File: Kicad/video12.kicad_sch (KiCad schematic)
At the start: 18 parts, among them J1201 DE15HD, U1201 THS7316, U1202 TPD7S019

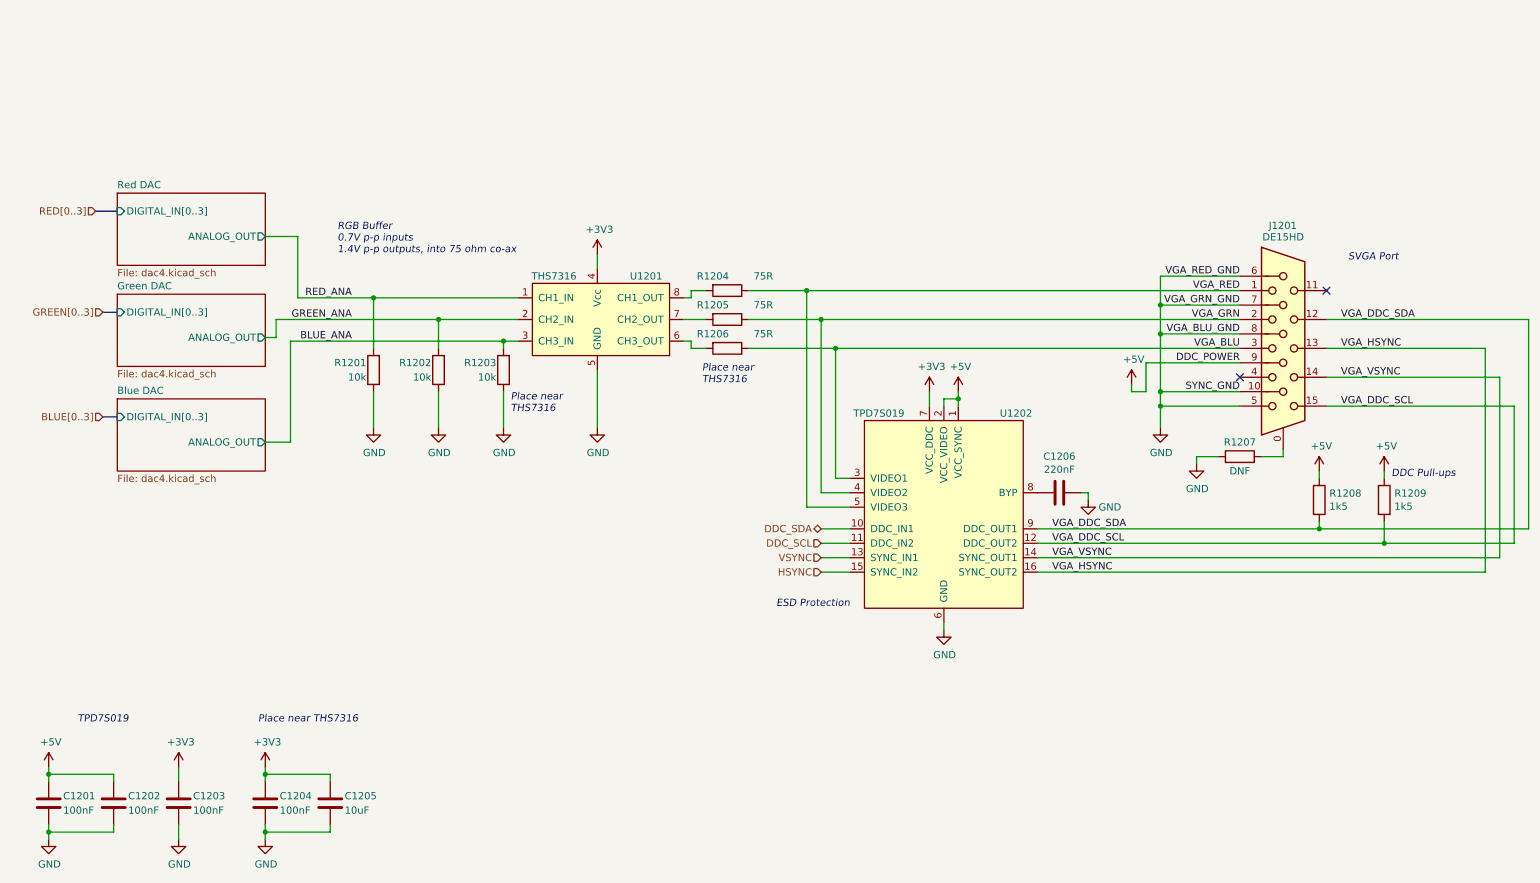
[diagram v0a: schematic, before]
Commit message: Update schematic files to Kicad 6.
Had to fix some symbols which didn't have perfect matches in K6.
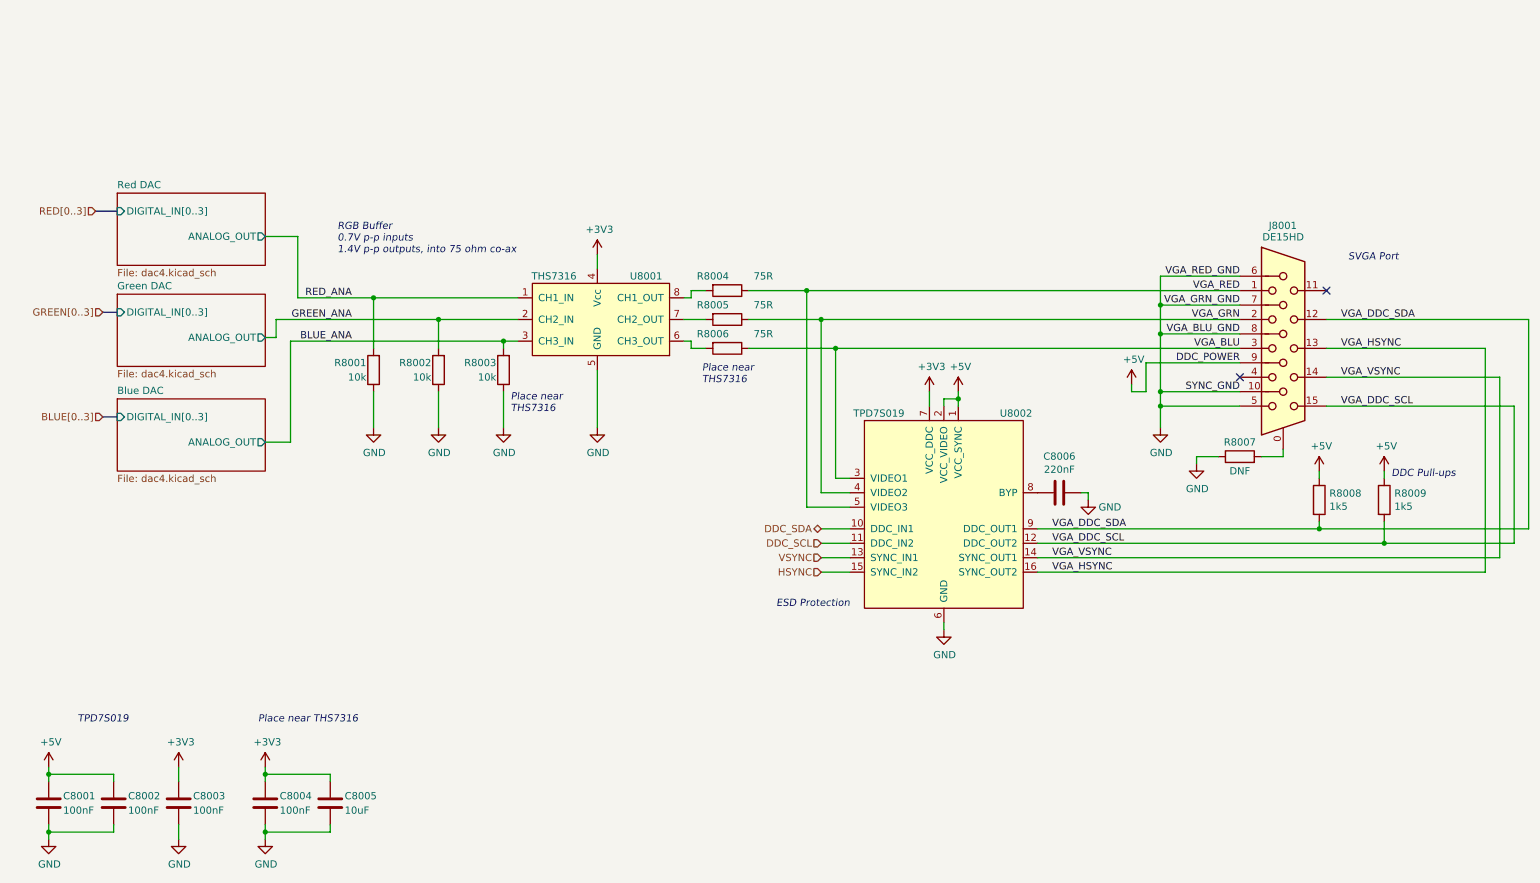
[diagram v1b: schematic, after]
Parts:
- renumbered C1201 to C8001, C1202 to C8002, C1203 to C8003, C1204 to C8004, C1205 to C8005, C1206 to C8006, J1201 to J8001, R1201 to R8001, R1202 to R8002, R1203 to R8003, R1204 to R8004, R1205 to R8005, R1206 to R8006, R1207 to R8007, R1208 to R8008, R1209 to R8009, U1201 to U8001, U1202 to U8002

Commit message: Imported sheets from Neotron Pico.
Standardised on +3V3 not +3.3V
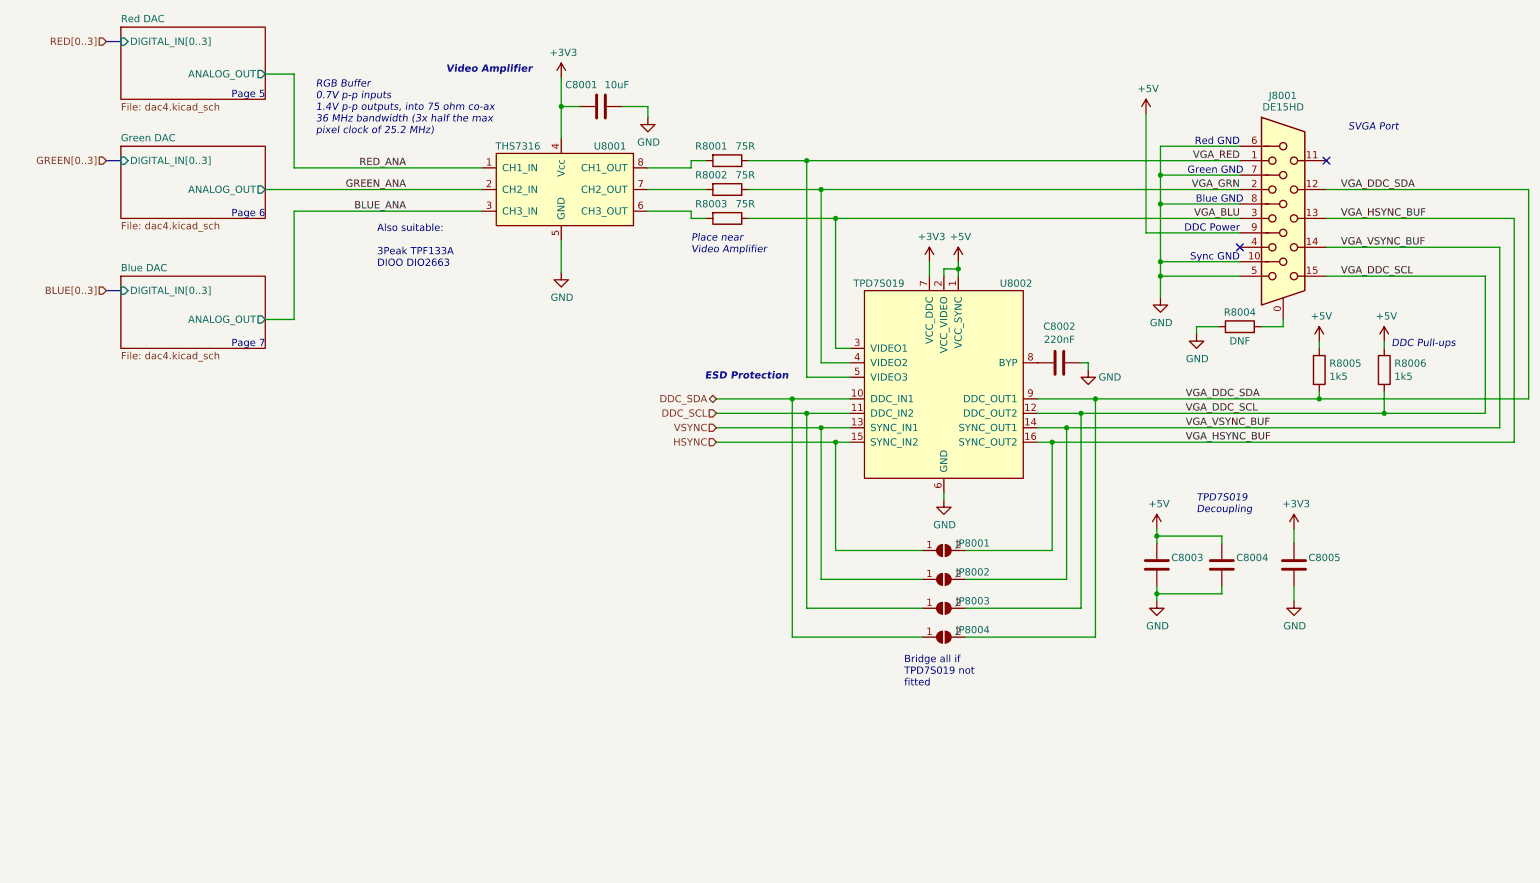
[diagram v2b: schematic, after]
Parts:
- removed C8001, C8002: 100nF, Capacitor_SMD:C_0805_2012Metric_Pad1.18x1.45mm_HandSolder, symbol Device:C
- removed R8001, R8002, R8003: 10k, Resistor_SMD:R_0805_2012Metric_Pad1.20x1.40mm_HandSolder, symbol Device:R
- added C8005: (no value), symbol Device:C
- added JP8001, JP8002, JP8003, JP8004: (no value), symbol Jumper:SolderJumper_2_Open
- C8001: renamed from C8005; JLCPCB Collection (none) -> Basic; MPN CPL-CAP-X5R-0805-10UF-16V -> CL21A106KAYNNNE; Manufacturer CPL -> Samsung; Voltage 10V -> 25V
- C8002: renamed from C8006; Digikey 1276-1093-1-ND -> (none); JLCPCB Collection (none) -> Basic; Tolerance X5R -> X7R
- C8003, C8004: value 100nF -> (none); footprint Capacitor_SMD:C_0805_2012Metric_Pad1.18x1.45mm_HandSolder -> (none); JLCPCB Collection (none) -> Basic; LCSC Part# C49678 -> C15850; MPN CPL-CAP-X7R-0805-100NF-50V -> CL21A106KAYNNNE; Manufacturer CPL -> Samsung; Voltage 10V -> 25V
- R8001: renamed from R8004; Digikey RMCF0805FT75R0-ND -> (none); JLCPCB Collection (none) -> Basic; MPN RMCF0805FT75R0 -> 0805W8F750JT5E; Manufacturer Stackpole -> Uniroyal
- R8002: renamed from R8005; Digikey RMCF0805FT75R0-ND -> (none); JLCPCB Collection (none) -> Basic; MPN RMCF0805FT75R0 -> 0805W8F750JT5E; Manufacturer Stackpole -> Uniroyal
- R8003: renamed from R8006; Digikey RMCF0805FT75R0-ND -> (none); JLCPCB Collection (none) -> Basic; MPN RMCF0805FT75R0 -> 0805W8F750JT5E; Manufacturer Stackpole -> Uniroyal
- R8005: renamed from R8008; Digikey RMCF0805FT1K50-ND -> (none); JLCPCB Collection (none) -> Basic; LCSC Part# C4310 -> C17604; MPN RMCF0805FT1K50 -> 0805W8F2001T5E; Manufacturer Stackpole -> Uniroyal
- R8006: renamed from R8009; Digikey RMCF0805FT1K50-ND -> (none); JLCPCB Collection (none) -> Basic; LCSC Part# C4310 -> C17604; MPN RMCF0805FT1K50 -> 0805W8F2001T5E; Manufacturer Stackpole -> Uniroyal
- U8001: Digikey 296-26684-1-ND -> (none); JLCPCB Collection (none) -> Extended; LCSC Part# C155446 -> C544774; MPN THS7316DR -> THS7316; Mouser 595-THS7316DR -> (none)
- U8002: Digikey 296-27595-1-ND -> (none); JLCPCB Collection (none) -> Extended; Mouser 595-TPD7S019-15DBQR -> (none)
- renumbered R8007 to R8004
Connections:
- net +3V3: now also C8005.2; no longer C8003.2, C8004.2
- net +5V: now also C8003.2, C8004.2
- net DDC_SCL: now also JP8003.1 (A)
- net DDC_SDA: now also JP8004.1 (A)
- net GND: now also C8005.1
- net HSYNC: now also JP8001.1 (A)
- net VGA_DDC_SCL: now also JP8003.2 (B)
- net VGA_DDC_SDA: now also JP8004.2 (B)
- net VSYNC: now also JP8002.1 (A)
- net VGA_HSYNC renamed VGA_HSYNC_BUF
- net VGA_HSYNC_BUF: now also JP8001.2 (B)
- net VGA_VSYNC renamed VGA_VSYNC_BUF
- net VGA_VSYNC_BUF: now also JP8002.2 (B)
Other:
- note added: "Also suitable: 3Peak TPF133A DIOO DIO2663"
- note added: "Blue GND"
- note added: "Bridge all if TPD7S019 not fitted"
- note added: "DDC Power"
- note added: "Green GND"
- note added: "Page 5"
- note added: "Page 6"
- note added: "Page 7"
- note added: "Place near Video Amplifier"
- note added: "RGB Buffer 0.7V p-p inputs 1.4V p-p outputs, into 75 ohm co-ax 36 MHz bandwidth (3x half the max pixel clock of 25.2 MHz)"
- note added: "Red GND"
- note added: "Sync GND"
- note added: "TPD7S019 Decoupling"
- note added: "Video Amplifier"
- note removed: "Place near THS7316"
- note removed: "RGB Buffer 0.7V p-p inputs 1.4V p-p outputs, into 75 ohm co-ax"
- note removed: "TPD7S019"
- company: https://neotron-compute.github.io/ -> https://neotron-compute.github.io
- moved on the sheet: C8001, C8002, J8001, R8001, R8002, R8003, R8004, R8005, R8006, U8001, U8002
